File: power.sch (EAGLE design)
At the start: 59 parts, among them J1 POWER_JACKPTH_BREAD, T1 SINGLE_NCHAN_FET, T2 SINGLE_NCHAN_FET, T3 SINGLE_NCHAN_FET, U1 MOSFET_PCHAN_20A, U14 MOSFET_PCHAN_20A, U2 MOSFET_PCHAN_20A

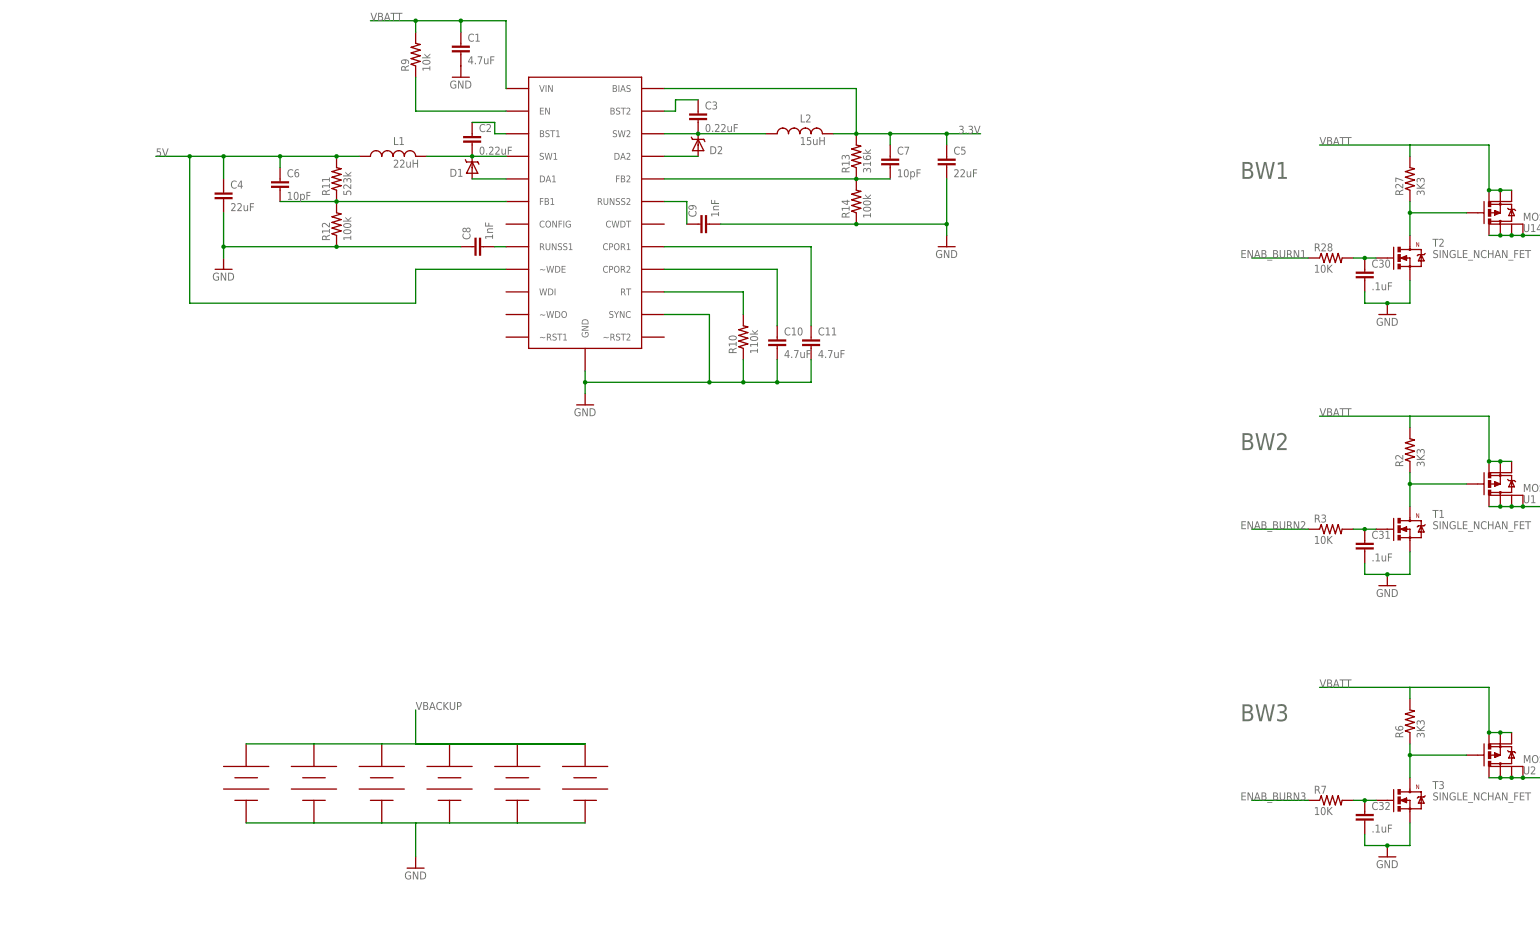
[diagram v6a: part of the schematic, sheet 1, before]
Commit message: Added current sensors to power board
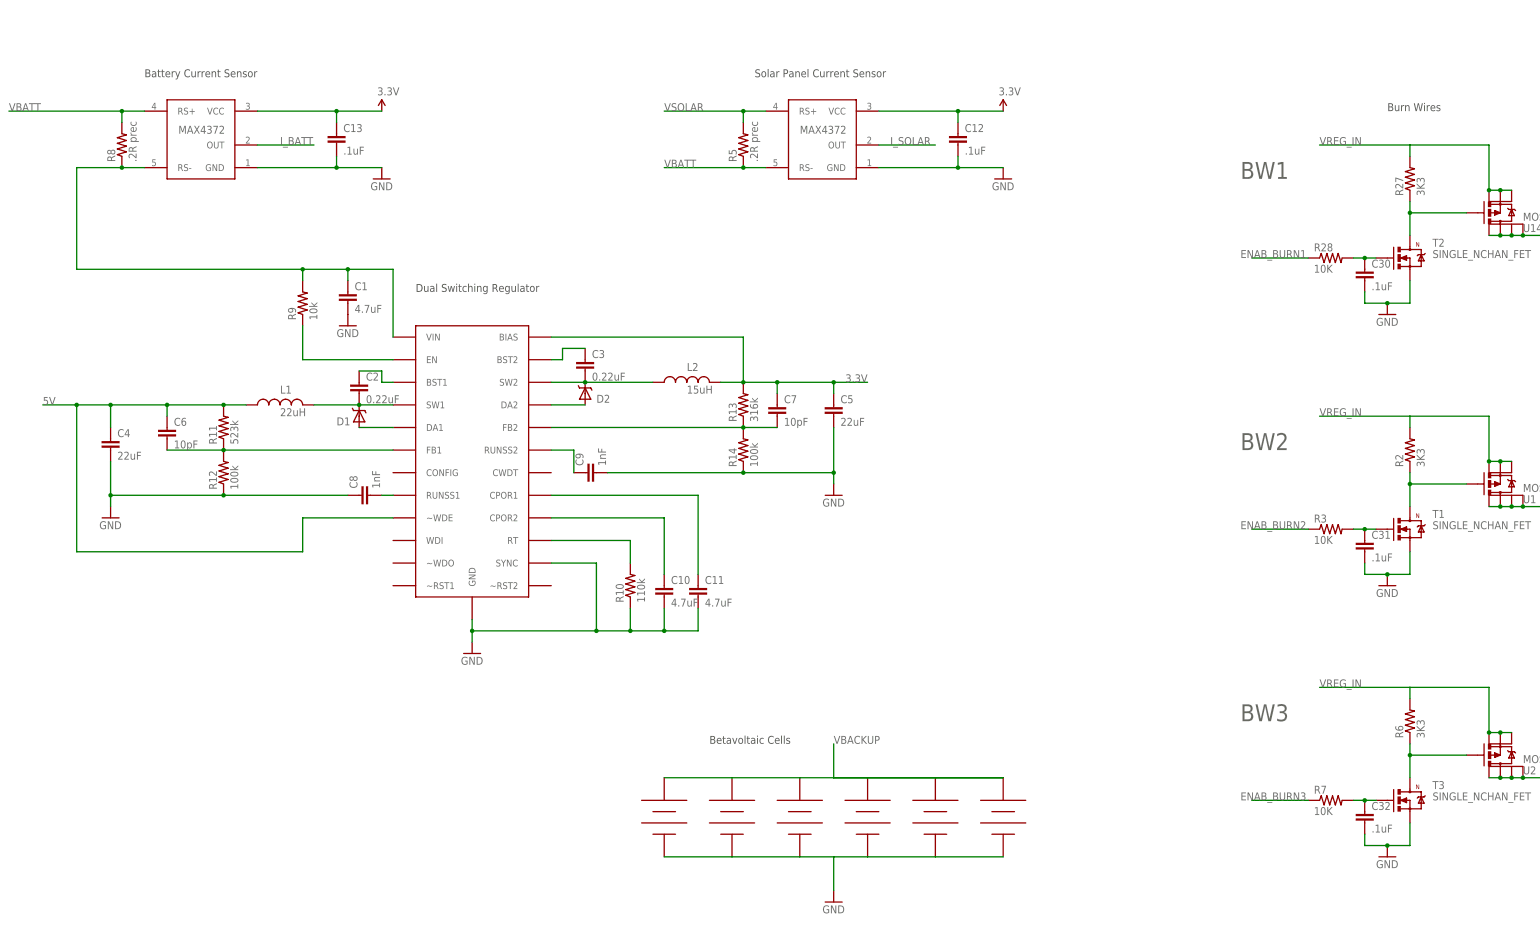
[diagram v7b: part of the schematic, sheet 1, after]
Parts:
- added C12, C13: .1uF, phonesat:CAP_0805
- added R5, R8: .2R prec, phonesat:RESISTOR0805
- added U$14, U$15: CURRENT_MAX4372, phonesat:CURRENT_MAX4372
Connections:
- new net I_BATT: U$15.OUT
- new net I_SOLAR: U$14.OUT
- new net VREG_IN: C1.1, H2.45, H2.46, JP5.1, R2.2, R27.2, R4.2, R6.2, R8.1, R9.2, U$13.VIN, U$15.RS-, U1.S@1, U1.S@2, U1.S@3, U14.S@1, U14.S@2, U14.S@3, U2.S@1, U2.S@2, U2.S@3
- net 3.3V: now also C12.1, C13.1, U$14.VCC, U$15.VCC
- net GND: now also C12.2, C13.2, U$14.GND, U$15.GND
- net VBATT: now also R5.1, R8.2, U$14.RS-, U$15.RS+; no longer C1.1, H2.45, H2.46, JP5.1, R2.2, R27.2, R4.2, R6.2, R9.2, U$13.VIN, U1.S@1, U1.S@2, U1.S@3, U14.S@1, U14.S@2, U14.S@3, U2.S@1, U2.S@2, U2.S@3
- net VSOLAR: now also R5.2, U$14.RS+
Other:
- note added: "Battery Current Sensor"
- note added: "Betavoltaic Cells"
- note added: "Burn Wires"
- note added: "Dual Switching Regulator"
- note added: "Option for 0, 1, or 2 footswitches"
- note added: "Solar Panel Current Sensor"
- note removed: "Optional for 0, 1, or 2 footswitches"
- moved on the sheet: C1, C10, C11, C2, C3, C4, C5, C6, C7, C8, C9, D1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

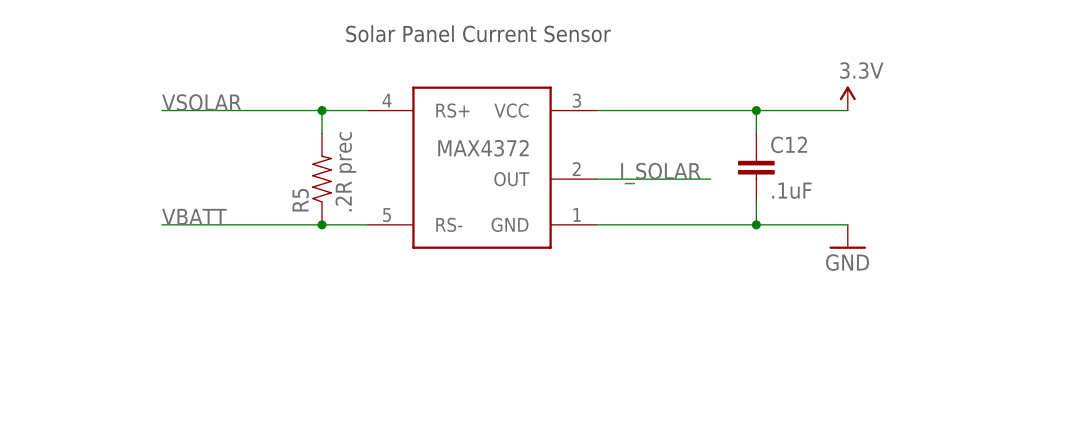
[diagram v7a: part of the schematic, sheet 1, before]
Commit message: Changed to all sparkfun library parts
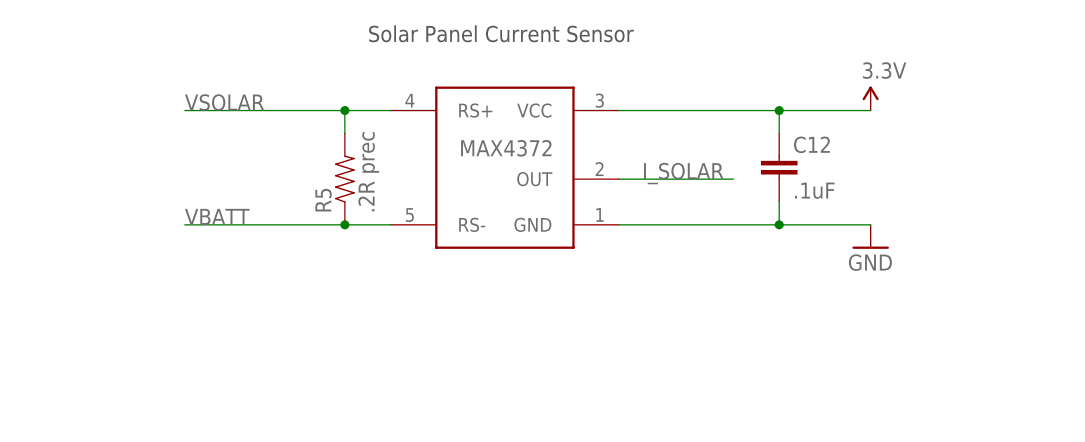
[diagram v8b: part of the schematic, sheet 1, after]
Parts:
- C12, C13: device phonesat:CAP_0805 -> SparkFun-Capacitors:CAP0805
- C30, C31, C32: device phonesat:CAPACITOR0805 -> SparkFun-Capacitors:CAP0805
- R2, R27, R28, R3, R5, R6, R7, R8: device phonesat:RESISTOR0805 -> SparkFun-Resistors:RESISTOR0805-RES
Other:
- moved on the sheet: C12, R5
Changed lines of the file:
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@@
 <part name="U14" library="phonesat" deviceset="MOSFET_PCHAN_20A" device=""/>
 <part name="T2" library="phonesat" deviceset="SINGLE_NCHAN_FET" device=""/>
-<part name="R27" library="phonesat" deviceset="RESISTOR" device="0805" value="3K3"/>
-<part name="C30" library="phonesat" deviceset="CAPACITOR" device="0805" value=".1uF"/>
-<part name="R28" library="phonesat" deviceset="RESISTOR" device="0805" value="10K"/>
+<part name="R27" library="SparkFun-Resistors" deviceset="RESISTOR" device="0805-RES" value="3K3"/>
+<part name="C30" library="SparkFun-Capacitors" deviceset="CAP" device="0805" value=".1uF"/>
+<part name="R28" library="SparkFun-Resistors" deviceset="RESISTOR" device="0805-RES" value="10K"/>
 <part name="GND1" library="SparkFun" deviceset="GND" device=""/>
 <part name="U1" library="phonesat" deviceset="MOSFET_PCHAN_20A" device=""/>
 <part name="T1" library="phonesat" deviceset="SINGLE_NCHAN_FET" device=""/>
-<part name="R2" library="phonesat" deviceset="RESISTOR" device="0805" value="3K3"/>
-<part name="C31" library="phonesat" deviceset="CAPACITOR" device="0805" value=".1uF"/>
-<part name="R3" library="phonesat" deviceset="RESISTOR" device="0805" value="10K"/>
+<part name="R2" library="SparkFun-Resistors" deviceset="RESISTOR" device="0805-RES" value="3K3"/>
+<part name="C31" library="SparkFun-Capacitors" deviceset="CAP" device="0805" value=".1uF"/>
+<part name="R3" library="SparkFun-Resistors" deviceset="RESISTOR" device="0805-RES" value="10K"/>
 <part name="GND7" library="SparkFun" deviceset="GND" device=""/>
 <part name="U2" library="phonesat" deviceset="MOSFET_PCHAN_20A" device=""/>
 <part name="T3" library="phonesat" deviceset="SINGLE_NCHAN_FET" device=""/>
-<part name="R6" library="phonesat" deviceset="RESISTOR" device="0805" value="3K3"/>
-<part name="C32" library="phonesat" deviceset="CAPACITOR" device="0805" value=".1uF"/>
-<part name="R7" library="phonesat" deviceset="RESISTOR" device="0805" value="10K"/>
+<part name="R6" library="SparkFun-Resistors" deviceset="RESISTOR" device="0805-RES" value="3K3"/>
+<part name="C32" library="SparkFun-Capacitors" deviceset="CAP" device="0805" value=".1uF"/>
+<part name="R7" library="SparkFun-Resistors" deviceset="RESISTOR" device="0805-RES" value="10K"/>
 <part name="GND8" library="SparkFun-Aesthetics" deviceset="GND" device=""/>
 <part name="GND9" library="SparkFun-Aesthetics" deviceset="GND" device=""/>
@@
 <part name="R4" library="rcl" deviceset="R-US_" device="R1210" value="0R"/>
 <part name="U$14" library="phonesat" deviceset="CURRENT_MAX4372" device=""/>
-<part name="R5" library="phonesat" deviceset="RESISTOR" device="0805" value=".2R prec"/>
-<part name="C12" library="phonesat" deviceset="CAP_0805" device="" value=".1uF"/>
+<part name="R5" library="SparkFun-Resistors" deviceset="RESISTOR" device="0805-RES" value=".2R prec"/>
+<part name="C12" library="SparkFun-Capacitors" deviceset="CAP" device="0805" value=".1uF"/>
 <part name="GND20" library="SparkFun" deviceset="GND" device=""/>
 <part name="P+1" library="SparkFun" deviceset="3.3V" device=""/>
 <part name="U$15" library="phonesat" deviceset="CURRENT_MAX4372" device=""/>
-<part name="C13" library="phonesat" deviceset="CAP_0805" device="" value=".1uF"/>
+<part name="C13" library="SparkFun-Capacitors" deviceset="CAP" device="0805" value=".1uF"/>
 <part name="GND21" library="SparkFun" deviceset="GND" device=""/>
 <part name="P+2" library="SparkFun" deviceset="3.3V" device=""/>
-<part name="R8" library="phonesat" deviceset="RESISTOR" device="0805" value=".2R prec"/>
+<part name="R8" library="SparkFun-Resistors" deviceset="RESISTOR" device="0805-RES" value=".2R prec"/>
 </parts>
 <sheets>
@@
 <text x="-48.26" y="-68.58" size="1.778" layer="97">Betavoltaic Cells</text>
 <text x="104.14" y="73.66" size="1.778" layer="97">Burn Wires</text>
-<text x="-38.1" y="81.28" size="1.778" layer="97">Solar Panel Current Sensor</text>
+<text x="-35.56" y="81.28" size="1.778" layer="97">Solar Panel Current Sensor</text>
 <text x="-175.26" y="81.28" size="1.778" layer="97">Battery Current Sensor</text>
 </plain>
@@
 <instance part="C10" gate="G$1" x="-58.42" y="-35.56"/>
 <instance part="C11" gate="G$1" x="-50.8" y="-35.56"/>
-<instance part="U$14" gate="G$1" x="-22.86" y="66.04"/>
-<instance part="R5" gate="G$1" x="-40.64" y="66.04" rot="R90"/>
-<instance part="C12" gate="G$1" x="7.62" y="66.04"/>
-<instance part="GND20" gate="1" x="17.78" y="58.42"/>
-<instance part="P+1" gate="G$1" x="17.78" y="73.66"/>
+<instance part="U$14" gate="G$1" x="-20.32" y="66.04"/>
+<instance part="R5" gate="G$1" x="-38.1" y="66.04" rot="R90"/>
+<instance part="C12" gate="G$1" x="10.16" y="66.04"/>
+<instance part="GND20" gate="1" x="20.32" y="58.42"/>
+<instance part="P+1" gate="G$1" x="20.32" y="73.66"/>
 <instance part="U$15" gate="G$1" x="-162.56" y="66.04"/>
 <instance part="C13" gate="G$1" x="-132.08" y="66.04"/>
@@
 </segment>
 <segment>
-<wire x1="-10.16" y1="60.96" x2="7.62" y2="60.96" width="0.1524" layer="91"/>
-<wire x1="7.62" y1="60.96" x2="7.62" y2="63.5" width="0.1524" layer="91"/>
-<wire x1="7.62" y1="60.96" x2="17.78" y2="60.96" width="0.1524" layer="91"/>
-<junction x="7.62" y="60.96"/>
+<wire x1="-7.62" y1="60.96" x2="10.16" y2="60.96" width="0.1524" layer="91"/>
+<wire x1="10.16" y1="60.96" x2="10.16" y2="63.5" width="0.1524" layer="91"/>
+<wire x1="10.16" y1="60.96" x2="20.32" y2="60.96" width="0.1524" layer="91"/>
+<junction x="10.16" y="60.96"/>
 <pinref part="U$14" gate="G$1" pin="GND"/>
 <pinref part="C12" gate="G$1" pin="2"/>
@@
 </segment>
 <segment>
-<wire x1="7.62" y1="71.12" x2="7.62" y2="73.66" width="0.1524" layer="91"/>
-<wire x1="7.62" y1="73.66" x2="-10.16" y2="73.66" width="0.1524" layer="91"/>
-<wire x1="7.62" y1="73.66" x2="17.78" y2="73.66" width="0.1524" layer="91"/>
-<junction x="7.62" y="73.66"/>
+<wire x1="10.16" y1="71.12" x2="10.16" y2="73.66" width="0.1524" layer="91"/>
+<wire x1="10.16" y1="73.66" x2="-7.62" y2="73.66" width="0.1524" layer="91"/>
+<wire x1="10.16" y1="73.66" x2="20.32" y2="73.66" width="0.1524" layer="91"/>
+<junction x="10.16" y="73.66"/>
 <pinref part="U$14" gate="G$1" pin="VCC"/>
 <pinref part="C12" gate="G$1" pin="1"/>
@@
 <net name="I_SOLAR" class="0">
 <segment>
-<wire x1="-10.16" y1="66.04" x2="2.54" y2="66.04" width="0.1524" layer="91"/>
-<label x="-7.62" y="66.04" size="1.778" layer="95"/>
+<wire x1="-7.62" y1="66.04" x2="5.08" y2="66.04" width="0.1524" layer="91"/>
+<label x="-5.08" y="66.04" size="1.778" layer="95"/>
 <pinref part="U$14" gate="G$1" pin="OUT"/>
 </segment>
@@
 <net name="VSOLAR" class="0">
 <segment>
-<wire x1="-35.56" y1="73.66" x2="-40.64" y2="73.66" width="0.1524" layer="91"/>
-<wire x1="-40.64" y1="73.66" x2="-40.64" y2="71.12" width="0.1524" layer="91"/>
-<wire x1="-40.64" y1="73.66" x2="-58.42" y2="73.66" width="0.1524" layer="91"/>
-<junction x="-40.64" y="73.66"/>
+<wire x1="-33.02" y1="73.66" x2="-38.1" y2="73.66" width="0.1524" layer="91"/>
+<wire x1="-38.1" y1="73.66" x2="-38.1" y2="71.12" width="0.1524" layer="91"/>
+<wire x1="-38.1" y1="73.66" x2="-55.88" y2="73.66" width="0.1524" layer="91"/>
+<junction x="-38.1" y="73.66"/>
 <pinref part="U$14" gate="G$1" pin="RS+"/>
 <pinref part="R5" gate="G$1" pin="2"/>
-<label x="-58.42" y="73.66" size="1.778" layer="95"/>
+<label x="-55.88" y="73.66" size="1.778" layer="95"/>
 </segment>
 </net>
@@
 </segment>
 <segment>
-<wire x1="-35.56" y1="60.96" x2="-40.64" y2="60.96" width="0.1524" layer="91"/>
-<wire x1="-40.64" y1="60.96" x2="-58.42" y2="60.96" width="0.1524" layer="91"/>
-<junction x="-40.64" y="60.96"/>
+<wire x1="-33.02" y1="60.96" x2="-38.1" y2="60.96" width="0.1524" layer="91"/>
+<wire x1="-38.1" y1="60.96" x2="-55.88" y2="60.96" width="0.1524" layer="91"/>
+<junction x="-38.1" y="60.96"/>
 <pinref part="U$14" gate="G$1" pin="RS-"/>
 <pinref part="R5" gate="G$1" pin="1"/>
-<label x="-58.42" y="60.96" size="1.778" layer="95"/>
-</segment>
-</net>
+<label x="-55.88" y="60.96" size="1.778" layer="95"/>
+</segment>
+</net>
